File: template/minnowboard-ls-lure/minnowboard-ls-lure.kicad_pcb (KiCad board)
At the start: 2 copper layers, 98.9 x 73.7 mm, 5 parts, among them P1 CONN_02X13

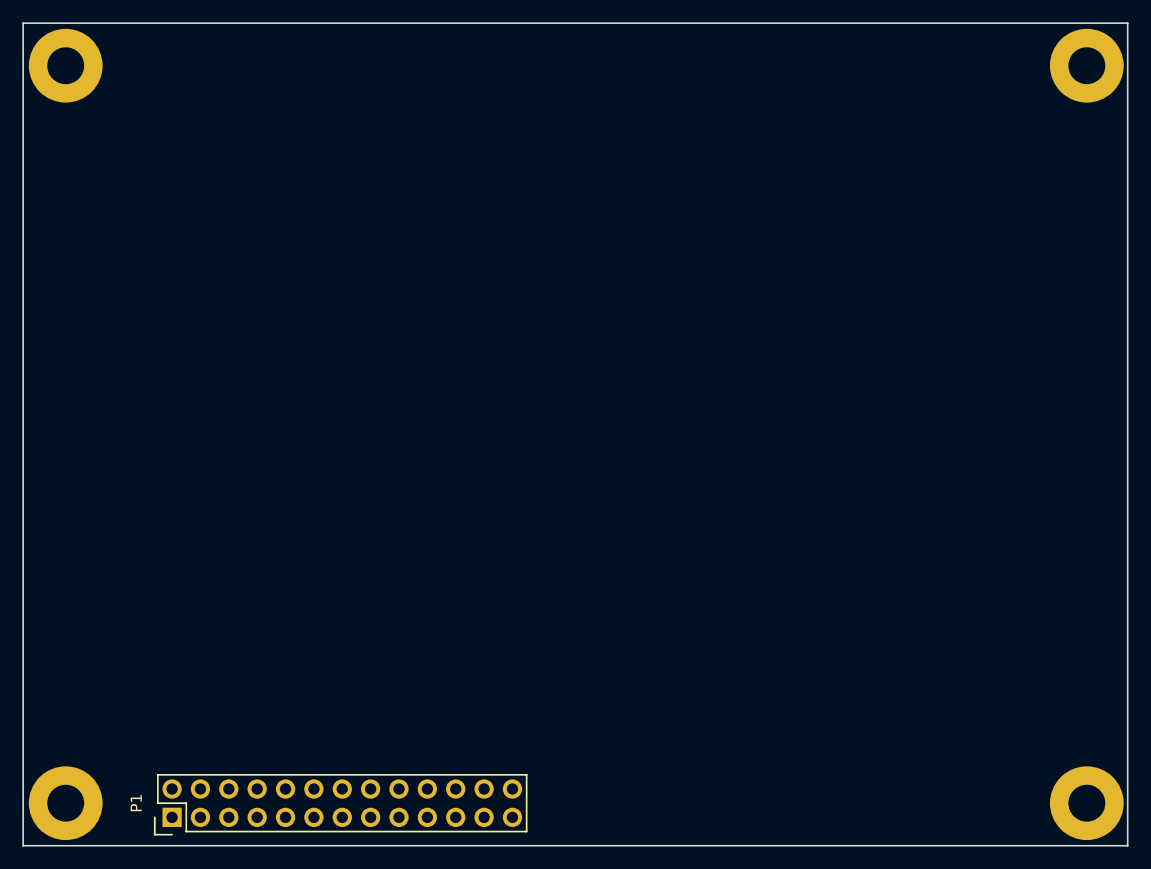
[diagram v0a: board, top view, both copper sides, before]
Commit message: Updates for the Minnowboard LS Lure template
- Switches to standard mounting holes.
- Removes local footprint library.
- Locks the mounting holes.
- Locks base board connector.
- Removes local library directory from project file.
- Denotes bottom side keepouts with Dwgs.User.
- Adds note in Cmts.User about keepouts.
- Updates image and html text.

Signed-off-by: Michael Welling <mwelling@ieee.org>
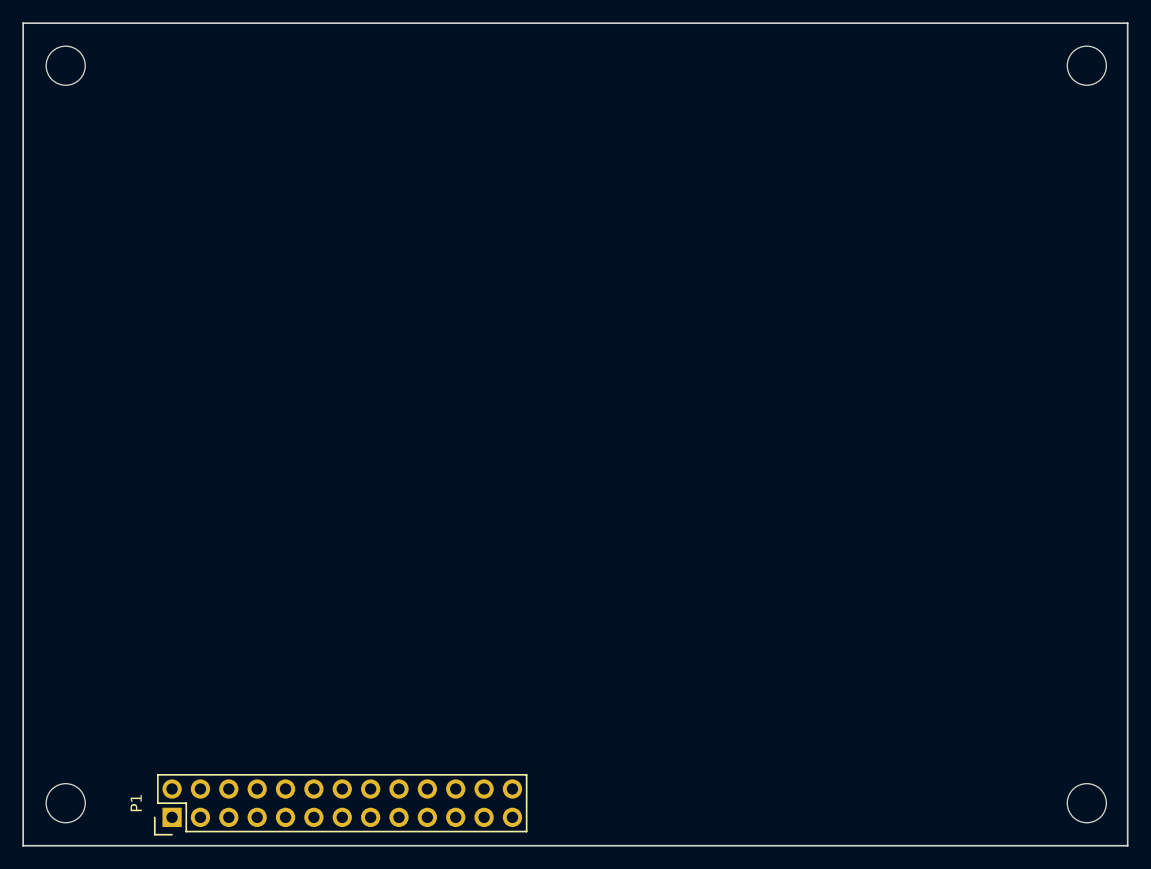
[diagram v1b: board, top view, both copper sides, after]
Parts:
- removed the REF** at (100.3, 141.0)
- removed the REF** at (100.3, 74.9)
- removed the REF** at (191.8, 74.9)
- removed the REF** at (191.8, 141.0)
- added REF**: MountingHole_3-5mm, Mounting_Holes:MountingHole_3-5mm, F.Cu at (191.8, 141.0)
- added REF**: MountingHole_3-5mm, Mounting_Holes:MountingHole_3-5mm, F.Cu at (100.3, 141.0)
- added REF**: MountingHole_3-5mm, Mounting_Holes:MountingHole_3-5mm, F.Cu at (100.3, 74.9)
- added REF**: MountingHole_3-5mm, Mounting_Holes:MountingHole_3-5mm, F.Cu at (191.8, 74.9)
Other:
- board text added: "NOTE: NO BOTTOM SIDE OR THROUGH-HOLE COMPONENTS IN THE AREAS DESIGNATED IN THE DWGS.USER LAYER TO AVOID COLLISION WITH MINNOWBOARD ETHERNET AND USB CONNECTORS."
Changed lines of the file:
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@@
     (area 96.444999 71.044999 195.502601 144.855001)
     (thickness 1.6)
-    (drawings 5)
+    (drawings 18)
     (tracks 0)
     (zones 0)
@@
     (add_net I2SMCLK_GPIO)
   )
-  (module Pin_Headers:Pin_Header_Straight_2x13 (layer F.Cu)
+  (module Pin_Headers:Pin_Header_Straight_2x13 locked (layer F.Cu)
     (at 109.855 142.24 90)
     (descr "Through hole pin header")
@@
       (effects (font (size 1 1) (thickness 0.15)))
     )
-    (fp_text value CONN_02X13 (at 5.08 3.175 180) (layer F.Fab)
+    (fp_text value CONN_02X13 (at 5.08 3.175 180) (layer F.Fab) hide
       (effects (font (size 1 1) (thickness 0.15)))
     )
@@
     )
   )
-  (module minnowboard-ls-lure:Mount (layer F.Cu)
+  (module Mounting_Holes:MountingHole_3-5mm locked (layer F.Cu)
+    (at 191.77 140.97)
+    (descr "Mounting hole, Befestigungsbohrung, 3,5mm, No Annular, Kein Restring,")
+    (tags "Mounting hole, Befestigungsbohrung, 3,5mm, No Annular, Kein Restring,")
+    (fp_text reference REF** (at 0 -4.50088) (layer F.SilkS) hide
+      (effects (font (size 1 1) (thickness 0.15)))
+    )
+    (fp_text value MountingHole_3-5mm (at 0 5.00126) (layer F.Fab) hide
+      (effects (font (size 1 1) (thickness 0.15)))
+    )
+    (fp_circle (center 0 0) (end 3.5 0) (layer Cmts.User) (width 0.381))
+    (pad 1 thru_hole circle (at 0 0) (size 3.5 3.5) (drill 3.5) (layers))
+  )
+  (module Mounting_Holes:MountingHole_3-5mm locked (layer F.Cu)
     (at 100.33 140.97)
-    (descr "module 1 pin (ou trou mecanique de percage)")
-    (tags DEV)
-    (fp_text reference REF** (at 0 -3.048) (layer F.SilkS) hide
-      (effects (font (size 1 1) (thickness 0.15)))
-    )
-    (fp_text value Mount (at 0 2.794) (layer F.Fab) hide
-      (effects (font (size 1 1) (thickness 0.15)))
-    )
-    (pad "" np_thru_hole circle (at 0 0) (size 6.604 6.604) (drill 3.302) (layers *.Cu *.Mask F.SilkS))
-  )
-  (module minnowboard-ls-lure:Mount (layer F.Cu)
+    (descr "Mounting hole, Befestigungsbohrung, 3,5mm, No Annular, Kein Restring,")
+    (tags "Mounting hole, Befestigungsbohrung, 3,5mm, No Annular, Kein Restring,")
+    (fp_text reference REF** (at 0 -4.50088) (layer F.SilkS) hide
+      (effects (font (size 1 1) (thickness 0.15)))
+    )
+    (fp_text value MountingHole_3-5mm (at 0 5.00126) (layer F.Fab) hide
+      (effects (font (size 1 1) (thickness 0.15)))
+    )
+    (fp_circle (center 0 0) (end 3.5 0) (layer Cmts.User) (width 0.381))
+    (pad 1 thru_hole circle (at 0 0) (size 3.5 3.5) (drill 3.5) (layers))
+  )
+  (module Mounting_Holes:MountingHole_3-5mm locked (layer F.Cu)
     (at 100.33 74.93)
-    (descr "module 1 pin (ou trou mecanique de percage)")
-    (tags DEV)
-    (fp_text reference REF** (at 0 -3.048) (layer F.SilkS) hide
-      (effects (font (size 1 1) (thickness 0.15)))
-    )
-    (fp_text value Mount (at 0 2.794) (layer F.Fab) hide
-      (effects (font (size 1 1) (thickness 0.15)))
-    )
-    (pad "" np_thru_hole circle (at 0 0) (size 6.604 6.604) (drill 3.302) (layers *.Cu *.Mask F.SilkS))
-  )
-  (module minnowboard-ls-lure:Mount (layer F.Cu)
+    (descr "Mounting hole, Befestigungsbohrung, 3,5mm, No Annular, Kein Restring,")
+    (tags "Mounting hole, Befestigungsbohrung, 3,5mm, No Annular, Kein Restring,")
+    (fp_text reference REF** (at 0 -4.50088) (layer F.SilkS) hide
+      (effects (font (size 1 1) (thickness 0.15)))
+    )
+    (fp_text value MountingHole_3-5mm (at 0 5.00126) (layer F.Fab) hide
+      (effects (font (size 1 1) (thickness 0.15)))
+    )
+    (fp_circle (center 0 0) (end 3.5 0) (layer Cmts.User) (width 0.381))
+    (pad 1 thru_hole circle (at 0 0) (size 3.5 3.5) (drill 3.5) (layers))
+  )
+  (module Mounting_Holes:MountingHole_3-5mm locked (layer F.Cu)
     (at 191.77 74.93)
-    (descr "module 1 pin (ou trou mecanique de percage)")
-    (tags DEV)
-    (fp_text reference REF** (at 0 -3.048) (layer F.SilkS) hide
-      (effects (font (size 1 1) (thickness 0.15)))
-    )
-    (fp_text value Mount (at 0 2.794) (layer F.Fab) hide
-      (effects (font (size 1 1) (thickness 0.15)))
-    )
-    (pad "" np_thru_hole circle (at 0 0) (size 6.604 6.604) (drill 3.302) (layers *.Cu *.Mask F.SilkS))
-  )
-  (module minnowboard-ls-lure:Mount (layer F.Cu)
-    (at 191.77 140.97)
-    (descr "module 1 pin (ou trou mecanique de percage)")
-    (tags DEV)
-    (fp_text reference REF** (at 0 -3.048) (layer F.SilkS) hide
-      (effects (font (size 1 1) (thickness 0.15)))
-    )
-    (fp_text value Mount (at 0 2.794) (layer F.Fab) hide
-      (effects (font (size 1 1) (thickness 0.15)))
-    )
-    (pad "" np_thru_hole circle (at 0 0) (size 6.604 6.604) (drill 3.302) (layers *.Cu *.Mask F.SilkS))
-  )
+    (descr "Mounting hole, Befestigungsbohrung, 3,5mm, No Annular, Kein Restring,")
+    (tags "Mounting hole, Befestigungsbohrung, 3,5mm, No Annular, Kein Restring,")
+    (fp_text reference REF** (at 0 -4.50088) (layer F.SilkS) hide
+      (effects (font (size 1 1) (thickness 0.15)))
+    )
+    (fp_text value MountingHole_3-5mm (at 0 5.00126) (layer F.Fab) hide
+      (effects (font (size 1 1) (thickness 0.15)))
+    )
+    (fp_circle (center 0 0) (end 3.5 0) (layer Cmts.User) (width 0.381))
+    (pad 1 thru_hole circle (at 0 0) (size 3.5 3.5) (drill 3.5) (layers))
+  )
+  (gr_text "NOTE: NO BOTTOM SIDE OR THROUGH-HOLE\nCOMPONENTS IN THE AREAS DESIGNATED IN THE\nDWGS.USER LAYER TO AVOID COLLISION WITH\nMINNOWBOARD ETHERNET AND USB CONNECTORS." (at 66.04 98.425) (layer Cmts.User)
+    (effects (font (size 1.5 1.5) (thickness 0.3)))
+  )
+  (gr_line (start 176.53 109.855) (end 195.58 90.805) (angle 90) (layer Dwgs.User) (width 0.2))
+  (gr_line (start 176.53 90.805) (end 195.58 109.855) (angle 90) (layer Dwgs.User) (width 0.2))
+  (gr_line (start 115.57 90.805) (end 96.52 109.855) (angle 90) (layer Dwgs.User) (width 0.2))
+  (gr_line (start 96.52 90.805) (end 115.57 109.855) (angle 90) (layer Dwgs.User) (width 0.2))
+  (gr_line (start 96.52 109.855) (end 96.52 90.805) (angle 90) (layer Dwgs.User) (width 0.2))
+  (gr_line (start 115.57 109.855) (end 96.52 109.855) (angle 90) (layer Dwgs.User) (width 0.2))
+  (gr_line (start 115.57 90.805) (end 115.57 109.855) (angle 90) (layer Dwgs.User) (width 0.2))
+  (gr_line (start 96.52 90.805) (end 115.57 90.805) (angle 90) (layer Dwgs.User) (width 0.2))
+  (gr_line (start 176.53 109.855) (end 176.53 90.805) (angle 90) (layer Dwgs.User) (width 0.2))
+  (gr_line (start 195.58 109.855) (end 176.53 109.855) (angle 90) (layer Dwgs.User) (width 0.2))
+  (gr_line (start 195.58 90.805) (end 195.58 109.855) (angle 90) (layer Dwgs.User) (width 0.2))
+  (gr_line (start 176.53 90.805) (end 195.58 90.805) (angle 90) (layer Dwgs.User) (width 0.2))
   (target plus (at 96.52 144.78) (size 5) (width 0.15) (layer Edge.Cuts))
   (gr_line (start 96.52 71.12) (end 96.52 144.78) (angle 90) (layer Edge.Cuts) (width 0.15))
@@
   (gr_line (start 195.4276 144.78) (end 195.4276 71.12) (angle 90) (layer Edge.Cuts) (width 0.15))
   (gr_line (start 96.52 144.78) (end 195.4276 144.78) (angle 90) (layer Edge.Cuts) (width 0.15))
-  (zone (net 0) (net_name "") (layer B.Cu) (hatch edge 0.508)
-    (connect_pads (clearance 0.508))
-    (min_thickness 0.254)
-    (keepout (tracks not_allowed) (vias not_allowed) (copperpour allowed))
-    (fill (arc_segments 16) (thermal_gap 0.508) (thermal_bridge_width 0.508))
-    (polygon
-      (pts
-        (xy 115.57 109.855) (xy 96.52 109.855) (xy 96.52 90.805) (xy 115.57 90.805) (xy 115.57 109.855)
-      )
-    )
-  )
-  (zone (net 0) (net_name "") (layer B.Cu) (hatch edge 0.508)
-    (connect_pads (clearance 0.508))
-    (min_thickness 0.254)
-    (keepout (tracks not_allowed) (vias not_allowed) (copperpour allowed))
-    (fill (arc_segments 16) (thermal_gap 0.508) (thermal_bridge_width 0.508))
-    (polygon
-      (pts
-        (xy 195.58 109.855) (xy 176.53 109.855) (xy 176.53 90.805) (xy 195.58 90.805)
-      )
-    )
-  )
 )

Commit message: Add new mounting hole symbols to schematic
Signed-off-by: Michael Welling <mwelling@ieee.org>
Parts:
- MK1, MK2, MK3, MK4: renamed from REF**; value MountingHole_3-5mm -> Mounting_Hole
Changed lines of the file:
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@@
     (descr "Mounting hole, Befestigungsbohrung, 3,5mm, No Annular, Kein Restring,")
     (tags "Mounting hole, Befestigungsbohrung, 3,5mm, No Annular, Kein Restring,")
-    (fp_text reference REF** (at 0 -4.50088) (layer F.SilkS) hide
+    (fp_text reference MK2 (at 0 -4.50088) (layer F.SilkS) hide
       (effects (font (size 1 1) (thickness 0.15)))
     )
-    (fp_text value MountingHole_3-5mm (at 0 5.00126) (layer F.Fab) hide
+    (fp_text value Mounting_Hole (at 0 5.00126) (layer F.Fab) hide
       (effects (font (size 1 1) (thickness 0.15)))
     )
@@
     (descr "Mounting hole, Befestigungsbohrung, 3,5mm, No Annular, Kein Restring,")
     (tags "Mounting hole, Befestigungsbohrung, 3,5mm, No Annular, Kein Restring,")
-    (fp_text reference REF** (at 0 -4.50088) (layer F.SilkS) hide
+    (fp_text reference MK1 (at 0 -4.50088) (layer F.SilkS) hide
       (effects (font (size 1 1) (thickness 0.15)))
     )
-    (fp_text value MountingHole_3-5mm (at 0 5.00126) (layer F.Fab) hide
+    (fp_text value Mounting_Hole (at 0 5.00126) (layer F.Fab) hide
       (effects (font (size 1 1) (thickness 0.15)))
     )
@@
     (descr "Mounting hole, Befestigungsbohrung, 3,5mm, No Annular, Kein Restring,")
     (tags "Mounting hole, Befestigungsbohrung, 3,5mm, No Annular, Kein Restring,")
-    (fp_text reference REF** (at 0 -4.50088) (layer F.SilkS) hide
+    (fp_text reference MK4 (at 0 -4.50088) (layer F.SilkS) hide
       (effects (font (size 1 1) (thickness 0.15)))
     )
-    (fp_text value MountingHole_3-5mm (at 0 5.00126) (layer F.Fab) hide
+    (fp_text value Mounting_Hole (at 0 5.00126) (layer F.Fab) hide
       (effects (font (size 1 1) (thickness 0.15)))
     )
@@
     (descr "Mounting hole, Befestigungsbohrung, 3,5mm, No Annular, Kein Restring,")
     (tags "Mounting hole, Befestigungsbohrung, 3,5mm, No Annular, Kein Restring,")
-    (fp_text reference REF** (at 0 -4.50088) (layer F.SilkS) hide
+    (fp_text reference MK3 (at 0 -4.50088) (layer F.SilkS) hide
       (effects (font (size 1 1) (thickness 0.15)))
     )
-    (fp_text value MountingHole_3-5mm (at 0 5.00126) (layer F.Fab) hide
+    (fp_text value Mounting_Hole (at 0 5.00126) (layer F.Fab) hide
       (effects (font (size 1 1) (thickness 0.15)))
     )
